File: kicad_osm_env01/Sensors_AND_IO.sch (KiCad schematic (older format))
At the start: 54 parts, among them J4 Conn_01x08, J8 STX-3000, Q5 FK3503010L, Q6 SSM3J328R, U10 ICS-43434, U11 HDC2080, U3 VEML7700-TT, U9 M74VHC1GT14DFT2G

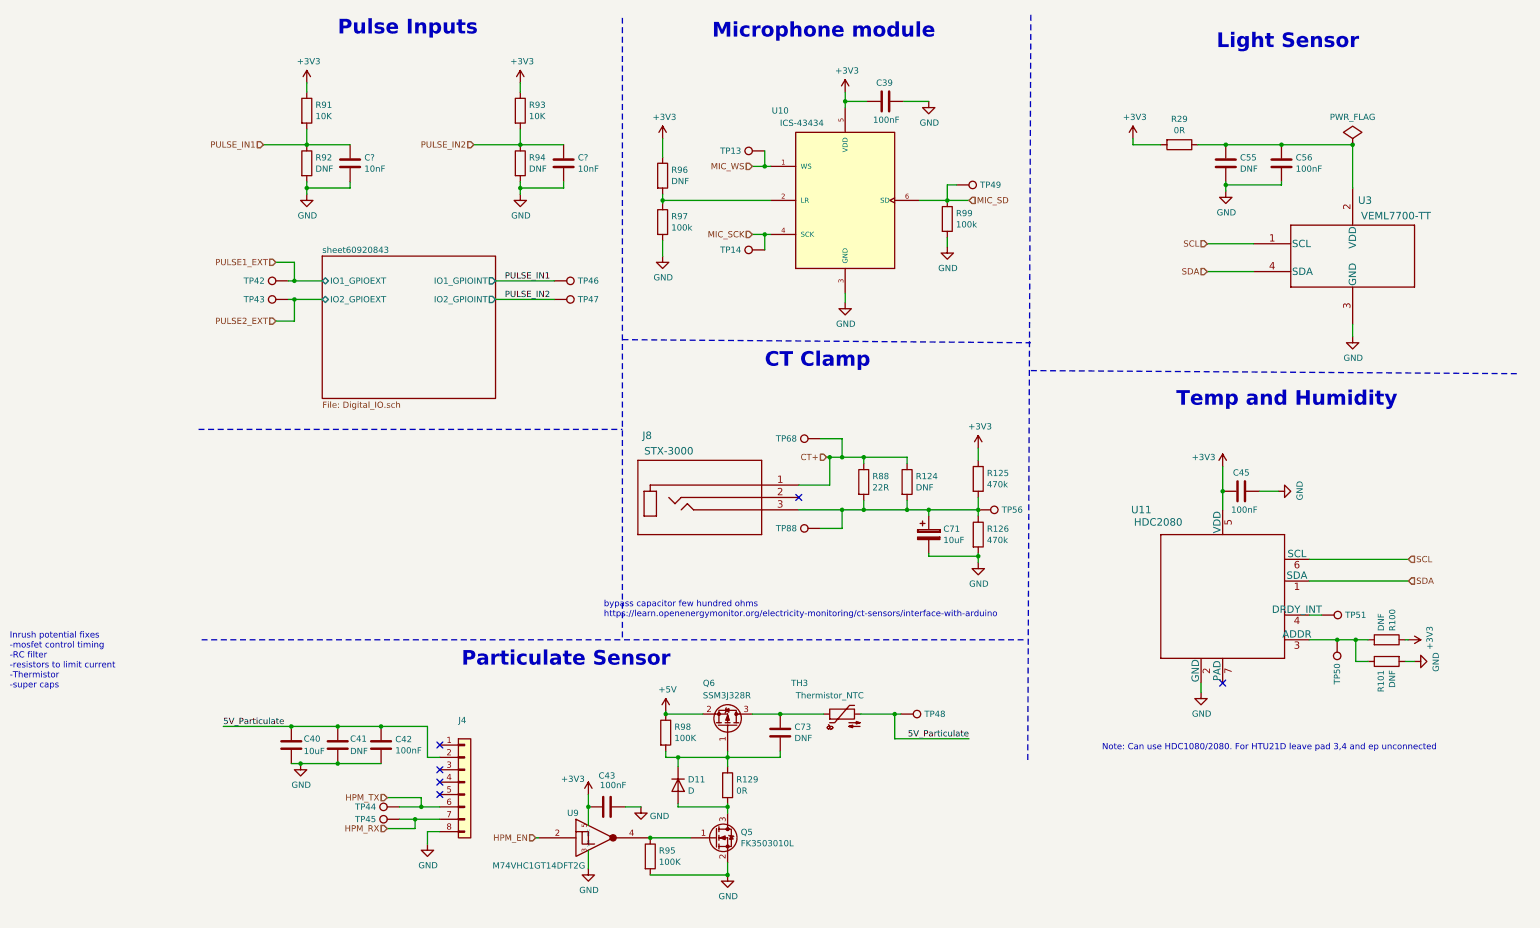
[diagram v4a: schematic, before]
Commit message: updated schematics
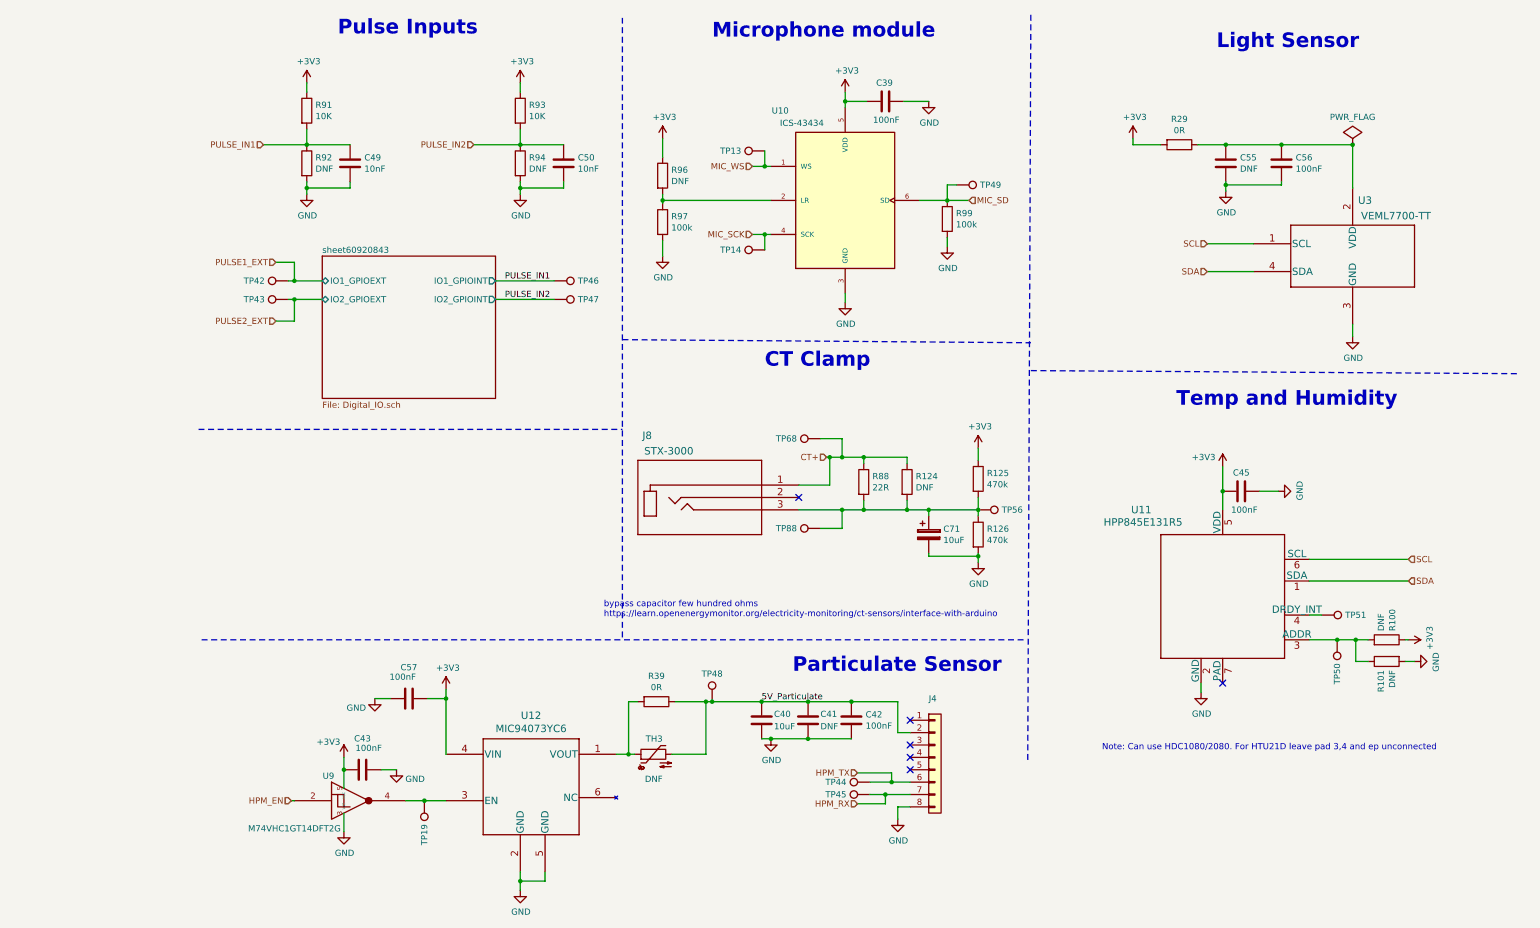
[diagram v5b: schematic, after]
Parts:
- removed C73: DNF, Capacitor_SMD:C_0603_1608Metric, symbol device:C
- removed D11: D, Diode_SMD:D_SOD-123, symbol device:D
- removed Q5: FK3503010L, Devtank_PCB_lib:SMini3-F2-B, symbol OSM_env01-rescue:2N7002-Transistor-ESP32-EVB_Rev_D-rescue
- removed Q6: SSM3J328R, Package_TO_SOT_SMD:SOT-23, symbol OSM_env01-rescue:NTR2101P-Transistor-ESP32-EVB_Rev_D-rescue
- removed R129: 0R, Resistor_SMD:R_0603_1608Metric, symbol OSM_env01-rescue:R-device-ESP32-EVB_Rev_D-rescue
- removed R95, R98: 100K, Resistor_SMD:R_0603_1608Metric, symbol OSM_env01-rescue:R-device-ESP32-EVB_Rev_D-rescue
- added C57: 100nF, Capacitor_SMD:C_0402_1005Metric, symbol OSM_env01-rescue:C-device-ESP32-EVB_Rev_D-rescue
- added R39: 0R, symbol device:R
- added TP19: Test_Point, TestPoint:TestPoint_Pad_D1.5mm, symbol OSM_env01-rescue:Test_Point-Connector-ESP32-EVB_Rev_D-rescue
- added U12: MIC94073YC6, Package_TO_SOT_SMD:SOT-363_SC-70-6, symbol Devtank:MIC94073YC6
- TH3: value Thermistor_NTC -> DNF; footprint Resistor_THT:R_Axial_DIN0204_L3.6mm_D1.6mm_P5.08mm_Horizontal -> Resistor_THT:R_Axial_DIN0617_L17.0mm_D6.0mm_P5.08mm_Vertical
- U11: value HDC2080 -> HPP845E131R5
- gave numbers to parts that had none: 2
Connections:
- net +3V3: now also C57.2, U12.4 (VIN)
- net 5V_Particulate: now also R39.1
- net GND: now also C57.1, U12.2 (GND), U12.5 (GND)
- net at TH3.1: now also R39.2, U12.1 (VOUT)
- net at U9.4: now also TP19.1, U12.3 (EN)
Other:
- note removed: "Inrush potential fixes\n-mosfet control timing\n-RC filter\n-resistors to limit current\n-Thermistor\n-super caps"
- moved on the sheet: C40, C41, C42, C43, J4, TH3, TP44, TP45, TP48, U9

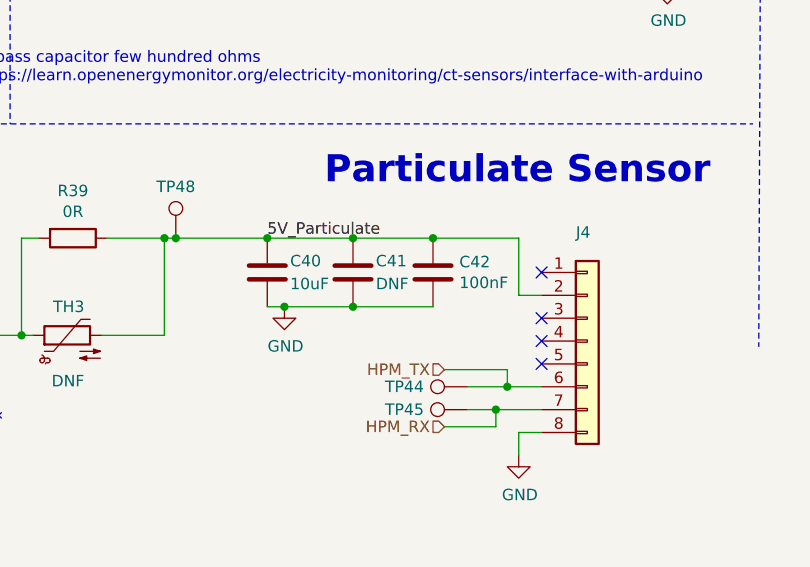
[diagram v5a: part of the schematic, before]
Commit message: added caps to particulate sensor
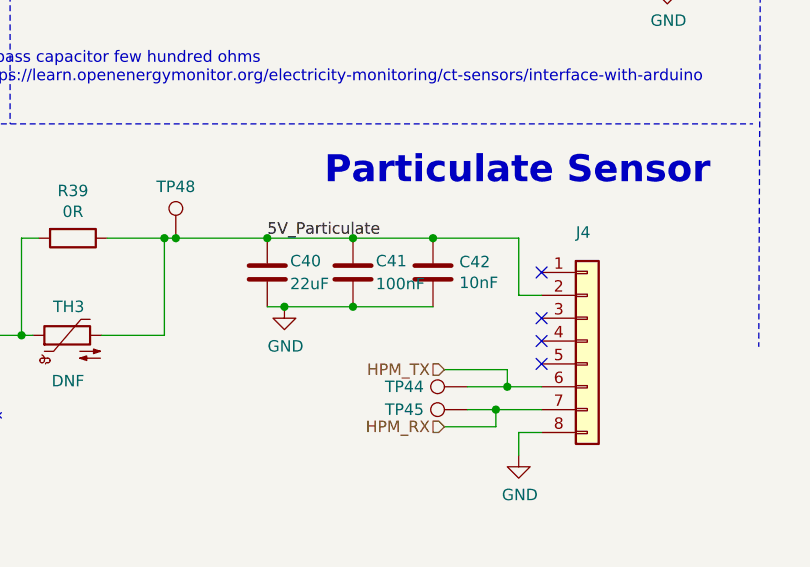
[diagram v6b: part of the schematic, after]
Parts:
- C40: value 10uF -> 22uF
- C41: value DNF -> 100nF
- C42: value 100nF -> 10nF
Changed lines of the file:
@@
 AR Path="/608F4675/609BB494" Ref="C40"  Part="1"
 F 0 "C40" H 5125 6250 50  0000 L CNN
-F 1 "10uF" H 5125 6150 50  0000 L CNN
+F 1 "22uF" H 5125 6150 50  0000 L CNN
 F 2 "Capacitor_SMD:C_0603_1608Metric" H 5063 6050 50  0001 C CNN
 F 3 "" H 5025 6200 50  0001 C CNN
@@
 AR Path="/608F4675/609BB49A" Ref="C41"  Part="1"
 F 0 "C41" H 5500 6250 50  0000 L CNN
-F 1 "DNF" H 5500 6150 50  0000 L CNN
+F 1 "100nF" H 5500 6150 50  0000 L CNN
 F 2 "Capacitor_SMD:C_0603_1608Metric" H 5438 6050 50  0001 C CNN
 F 3 "" H 5400 6200 50  0001 C CNN
@@
 AR Path="/608F4675/609BB4A0" Ref="C42"  Part="1"
 F 0 "C42" H 5865 6246 50  0000 L CNN
-F 1 "100nF" H 5865 6155 50  0000 L CNN
+F 1 "10nF" H 5865 6155 50  0000 L CNN
 F 2 "Capacitor_SMD:C_0402_1005Metric" H 5788 6050 50  0001 C CNN
 F 3 "" H 5750 6200 50  0001 C CNN

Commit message: Updated schematics
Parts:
- removed C43: 100nF, Capacitor_SMD:C_0402_1005Metric, symbol OSM_env01-rescue:C-device-ESP32-EVB_Rev_D-rescue
- removed U9: M74VHC1GT14DFT2G, Package_TO_SOT_SMD:SOT-353_SC-70-5, symbol OSM_env01-rescue:NL17SZ14-Devtank-ESP32-EVB_Rev_D-rescue
- added L3: 2A/0.05DCR, Inductor_SMD:L_0402_1005Metric, symbol device:Ferrite_Bead
- added R40: 100k, symbol device:R
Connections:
- net +3V3: now also L3.1; no longer C39.2, C57.2, U10.5 (VDD), U12.4 (VIN)
- net GND: now also R40.2
- net HPM_EN: now also TP19.1, U12.3 (EN), R40.1
- new net: C39.2, L3.2, U10.5 (VDD)
- new net +5V: C57.2, U12.4 (VIN)
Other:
- moved on the sheet: C39, C40, C41, C42, C57, J4, R39, R96, R97, R99, TH3, TP13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

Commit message: rough throwdown of all parts
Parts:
- removed TP19, TP88: Test_Point, TestPoint:TestPoint_Pad_D1.5mm, symbol OSM_env01-rescue:Test_Point-Connector-ESP32-EVB_Rev_D-rescue
- C40: footprint Capacitor_SMD:C_0603_1608Metric -> Capacitor_SMD:C_0805_2012Metric
- C41: footprint Capacitor_SMD:C_0603_1608Metric -> Capacitor_SMD:C_0402_1005Metric
- C49, C50: footprint (none) -> Capacitor_SMD:C_0402_1005Metric
- R39, R40: footprint (none) -> Resistor_SMD:R_0603_1608Metric
- R91, R93: value 10K -> 10k
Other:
- moved on the sheet: TP56
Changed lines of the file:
@@
 AR Path="/608F4675/6092084A" Ref="R91"  Part="1"
 F 0 "R91" H 1420 1321 50  0000 L CNN
-F 1 "10K" H 1420 1230 50  0000 L CNN
+F 1 "10k" H 1420 1230 50  0000 L CNN
 F 2 "Resistor_SMD:R_0603_1608Metric" V 1280 1275 50  0001 C CNN
 F 3 "" H 1350 1275 50  0001 C CNN
@@
 AR Path="/608F4675/6092088E" Ref="R93"  Part="1"
 F 0 "R93" H 3145 1321 50  0000 L CNN
-F 1 "10K" H 3145 1230 50  0000 L CNN
+F 1 "10k" H 3145 1230 50  0000 L CNN
 F 2 "Resistor_SMD:R_0603_1608Metric" V 3005 1275 50  0001 C CNN
 F 3 "" H 3075 1275 50  0001 C CNN
@@
 F 0 "C40" H 4700 6225 50  0000 L CNN
 F 1 "22uF" H 4700 6125 50  0000 L CNN
-F 2 "Capacitor_SMD:C_0603_1608Metric" H 4638 6025 50  0001 C CNN
+F 2 "Capacitor_SMD:C_0805_2012Metric" H 4638 6025 50  0001 C CNN
 F 3 "" H 4600 6175 50  0001 C CNN
 	1    4600 6175
@@
 F 0 "C41" H 5125 6225 50  0000 L CNN
 F 1 "100nF" H 5125 6125 50  0000 L CNN
-F 2 "Capacitor_SMD:C_0603_1608Metric" H 5063 6025 50  0001 C CNN
+F 2 "Capacitor_SMD:C_0402_1005Metric" H 5063 6025 50  0001 C CNN
 F 3 "" H 5025 6175 50  0001 C CNN
 	1    5025 6175
@@
 	5850 4075 5675 4075
 Wire Wire Line
-	6200 4125 6200 4075
-Wire Wire Line
 	6200 4500 6200 4425
 Wire Wire Line
@@
 	0    -1   1    0
 $EndComp
-$Comp
-L OSM_env01-rescue:Test_Point-Connector-ESP32-EVB_Rev_D-rescue TP?
-U 1 1 612C3073
-P 5500 4650
-AR Path="/5F6F7717/612C3073" Ref="TP?"  Part="1"
-AR Path="/612C3073" Ref="TP?"  Part="1"
-AR Path="/608F4675/612C3073" Ref="TP88"  Part="1"
-F 0 "TP88" V 5500 4925 50  0000 C CNN
-F 1 "Test_Point" V 5575 4875 50  0001 C CNN
-F 2 "TestPoint:TestPoint_Pad_D1.5mm" H 5700 4650 50  0001 C CNN
-F 3 "~" H 5700 4650 50  0001 C CNN
-	1    5500 4650
-	0    -1   1    0
-$EndComp
-Wire Wire Line
-	5500 4650 5675 4650
-Wire Wire Line
-	5675 4650 5675 4500
 Wire Wire Line
 	5675 4075 5675 3925
-Wire Wire Line
-	5675 3925 5500 3925
 Connection ~ 5675 4075
 Wire Wire Line
@@
 	1    0    0    -1
 $EndComp
-Wire Wire Line
-	5675 4500 5850 4500
 Connection ~ 6200 4500
 Wire Wire Line
@@
 Wire Wire Line
 	5850 4125 5850 4075
-Wire Wire Line
-	6200 4075 5850 4075
-Connection ~ 5850 4075
 $Comp
 L Devtank:STX-3000 J8
@@
 PULSE_IN2
 Wire Wire Line
-	5325 4500 5675 4500
-Wire Wire Line
-	5325 4300 5575 4300
-Wire Wire Line
 	5575 4300 5575 4075
 Connection ~ 5575 4075
@@
 	5575 4075 5550 4075
 NoConn ~ 5325 4400
-Connection ~ 5675 4500
 $Comp
 L device:R R29
@@
 Wire Wire Line
 	9800 3100 9800 3000
-Wire Wire Line
-	8625 2575 9000 2575
 Text HLabel 8625 2575 0    50   Input ~ 0
 SDA
-Wire Wire Line
-	9000 2350 8625 2350
 Text HLabel 8625 2350 0    50   Input ~ 0
 SCL
@@
 L OSM_env01-rescue:Test_Point-Connector-ESP32-EVB_Rev_D-rescue TP?
 U 1 1 61DFE85D
-P 6775 4500
+P 6825 4500
 AR Path="/5F6F7717/61DFE85D" Ref="TP?"  Part="1"
 AR Path="/61DFE85D" Ref="TP?"  Part="1"
 AR Path="/608F4675/61DFE85D" Ref="TP56"  Part="1"
-F 0 "TP56" V 6775 4775 50  0000 C CNN
-F 1 "Test_Point" V 6850 4725 50  0001 C CNN
-F 2 "TestPoint:TestPoint_Pad_D1.5mm" H 6975 4500 50  0001 C CNN
-F 3 "~" H 6975 4500 50  0001 C CNN
-	1    6775 4500
+F 0 "TP56" V 6825 4775 50  0000 C CNN
+F 1 "Test_Point" V 6900 4725 50  0001 C CNN
+F 2 "TestPoint:TestPoint_Pad_D1.5mm" H 7025 4500 50  0001 C CNN
+F 3 "~" H 7025 4500 50  0001 C CNN
+	1    6825 4500
 	0    1    1    0
 $EndComp
@@
 F 0 "C49" H 1815 1746 50  0000 L CNN
 F 1 "10nF" H 1815 1655 50  0000 L CNN
-F 2 "" H 1738 1550 50  0001 C CNN
+F 2 "Capacitor_SMD:C_0402_1005Metric" H 1738 1550 50  0001 C CNN
 F 3 "" H 1700 1700 50  0001 C CNN
 	1    1700 1700
@@
 F 0 "C50" H 3540 1746 50  0000 L CNN
 F 1 "10nF" H 3540 1655 50  0000 L CNN
-F 2 "" H 3463 1550 50  0001 C CNN
+F 2 "Capacitor_SMD:C_0402_1005Metric" H 3463 1550 50  0001 C CNN
 F 3 "" H 3425 1700 50  0001 C CNN
 	1    3425 1700
@@
 F 0 "R39" V 3775 6025 50  0000 C CNN
 F 1 "0R" V 3950 6025 50  0000 C CNN
-F 2 "" V 3805 6025 50  0001 C CNN
+F 2 "Resistor_SMD:R_0603_1608Metric" V 3805 6025 50  0001 C CNN
 F 3 "" H 3875 6025 50  0001 C CNN
 	1    3875 6025
@@
 $Comp
 L OSM_env01-rescue:Test_Point-Connector-ESP32-EVB_Rev_D-rescue TP?
-U 1 1 6176A132
-P 1750 6700
-AR Path="/5F6F7717/6176A132" Ref="TP?"  Part="1"
-AR Path="/6176A132" Ref="TP?"  Part="1"
-AR Path="/608F4675/6176A132" Ref="TP19"  Part="1"
-F 0 "TP19" V 1750 6975 50  0000 C CNN
-F 1 "Test_Point" V 1825 6925 50  0001 C CNN
-F 2 "TestPoint:TestPoint_Pad_D1.5mm" H 1950 6700 50  0001 C CNN
-F 3 "~" H 1950 6700 50  0001 C CNN
-	1    1750 6700
-	0    -1   -1   0
-$EndComp
-$Comp
-L OSM_env01-rescue:Test_Point-Connector-ESP32-EVB_Rev_D-rescue TP?
 U 1 1 60A49311
 P 4325 6025
@@
 F 0 "R40" H 1970 7021 50  0000 L CNN
 F 1 "100k" H 1970 6930 50  0000 L CNN
-F 2 "" V 1830 6975 50  0001 C CNN
+F 2 "Resistor_SMD:R_0603_1608Metric" V 1830 6975 50  0001 C CNN
 F 3 "" H 1900 6975 50  0001 C CNN
 	1    1900 6975
 	1    0    0    -1
 $EndComp
-Wire Wire Line
-	1650 6825 1825 6825
 Connection ~ 1900 6825
 Wire Wire Line
 	1900 6825 2175 6825
-Wire Wire Line
-	1750 6700 1825 6700
-Wire Wire Line
-	1825 6700 1825 6825
-Connection ~ 1825 6825
-Wire Wire Line
-	1825 6825 1900 6825
 $Comp
 L OSM_env01:GND #PWR0149
@@
 Wire Wire Line
 	5625 1200 6325 1200
+Wire Wire Line
+	8625 2350 9000 2350
+Wire Wire Line
+	9000 2575 8625 2575
+Wire Wire Line
+	6200 4125 6200 4075
+Wire Wire Line
+	6200 4075 5850 4075
+Connection ~ 5850 4075
+Wire Wire Line
+	5675 3925 5500 3925
+Wire Wire Line
+	5325 4300 5575 4300
+Wire Wire Line
+	6825 4500 6775 4500
+Wire Wire Line
+	5325 4500 5850 4500
+Wire Wire Line
+	1650 6825 1900 6825
 $EndSCHEMATC
